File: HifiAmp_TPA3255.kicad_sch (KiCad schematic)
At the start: 111 parts, among them J1 PVDD 48V IN — NEEDS_DATA, J2 RCA L SE, J3 RCA R SE, J301 SPK_L, J302 SPK_R, Q301 NEEDS_DATA, U1 LM5010ASD, U2 LM2940IMP-12/NOPB, U3 TLV1117-33IDCY, U4 OPA1612AIDR, U5 OPA1612AIDR, U6 TPA3255B, U7 TPS3802K33DCKR

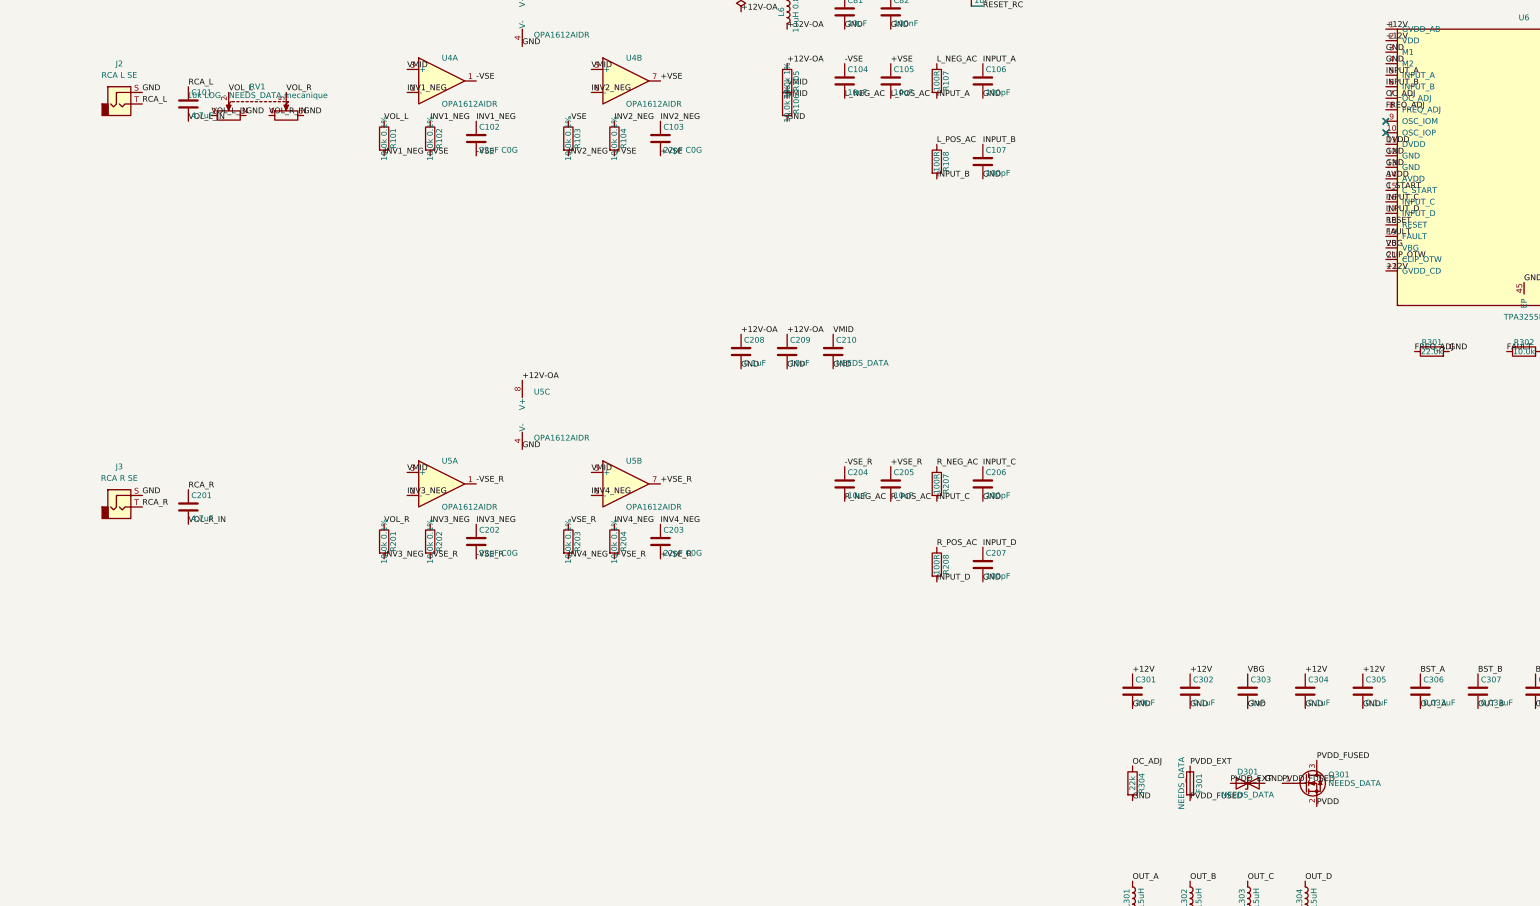
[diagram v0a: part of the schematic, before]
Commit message: feat(schematic): remote RV1/J2/J3, fix Q301 into a correct P-MOS (B2.1-B2.4)
J2/J3 become Conn_01x02 for chassis-mounted RCA, J4 (Conn_01x06) carries
the six volume nets for the remote pot, and Q301 is requalified from
N-MOS to P-MOS with a proper gate network (R305 100k to GND, D302 15 V
zener).

The first correction wired the P-MOS source upstream. A P-MOS body diode
has its anode on the drain, which must therefore sit upstream to conduct
in the normal direction; wired the other way the diode goes forward
during a polarity reversal and the protection does nothing. Verified
after fix by reading the symbol geometry: S carries PVDD, D carries
PVDD_FUSED, D302 cathode on PVDD. ERC cannot see this class of defect.

ERC re-gate: 0 errors / 14 warnings, 4 library mismatches + 10 off-grid,
same split as the C1 reference.

B2.1 stays open: no MCP tool exposes the on_board attribute, so RV1 is
still on the board (tracked as B2.8).

Co-Authored-By: Claude Opus 5 <noreply@anthropic.com>
Claude-Session: https://claude.ai/code/session_01NbP75MQx5stMnq6BjDMVex
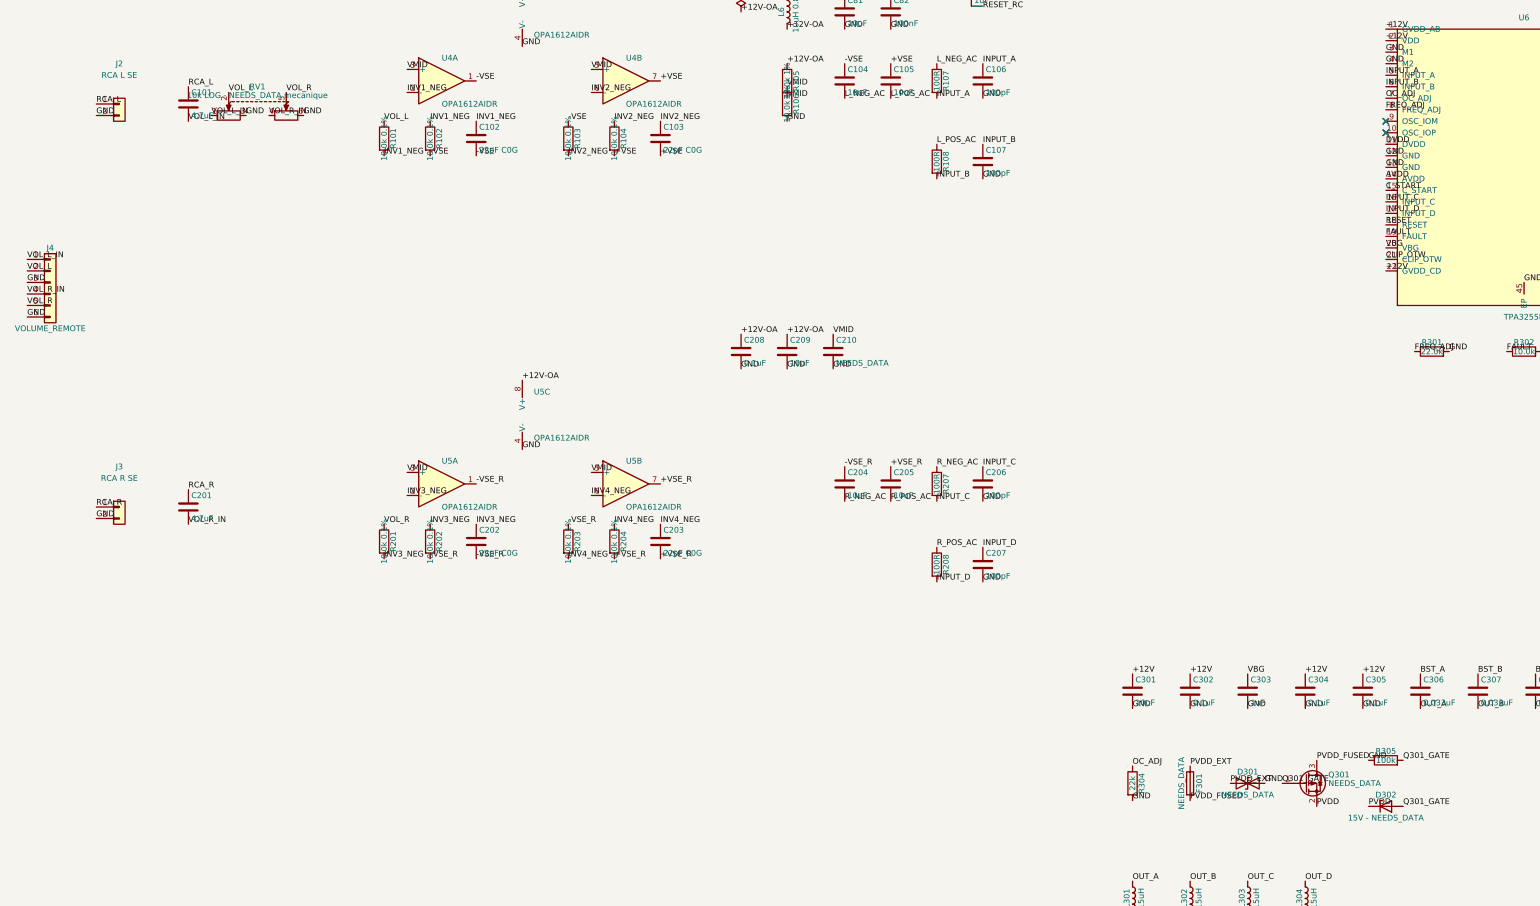
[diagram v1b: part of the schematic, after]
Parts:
- added D302: 15V - NEEDS_DATA, symbol Device:D_Zener
- added J4: VOLUME_REMOTE, symbol Connector_Generic:Conn_01x06
- added R305: 100k, symbol Device:R
- J2, J3: symbol Connector_Audio:AudioJack2 -> Connector_Generic:Conn_01x02
- Q301: symbol Transistor_FET:Q_NMOS_GSD -> Transistor_FET:Q_PMOS_GSD
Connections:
- net GND: now also J2.2 (Pin_2), J3.2 (Pin_2), J4.3 (Pin_3), J4.6 (Pin_6), R305.1; no longer J2.S, J3.S
- net PVDD: now also D302.1 (K)
- net PVDD_FUSED: no longer Q301.1 (G)
- net RCA_L: now also J2.1 (Pin_1); no longer J2.T
- net RCA_R: now also J3.1 (Pin_1); no longer J3.T
- net VOL_L: now also J4.2 (Pin_2)
- net VOL_L_IN: now also J4.1 (Pin_1)
- net VOL_R: now also J4.5 (Pin_5)
- net VOL_R_IN: now also J4.4 (Pin_4)
- new net Q301_GATE: D302.2 (A), Q301.1 (G), R305.2

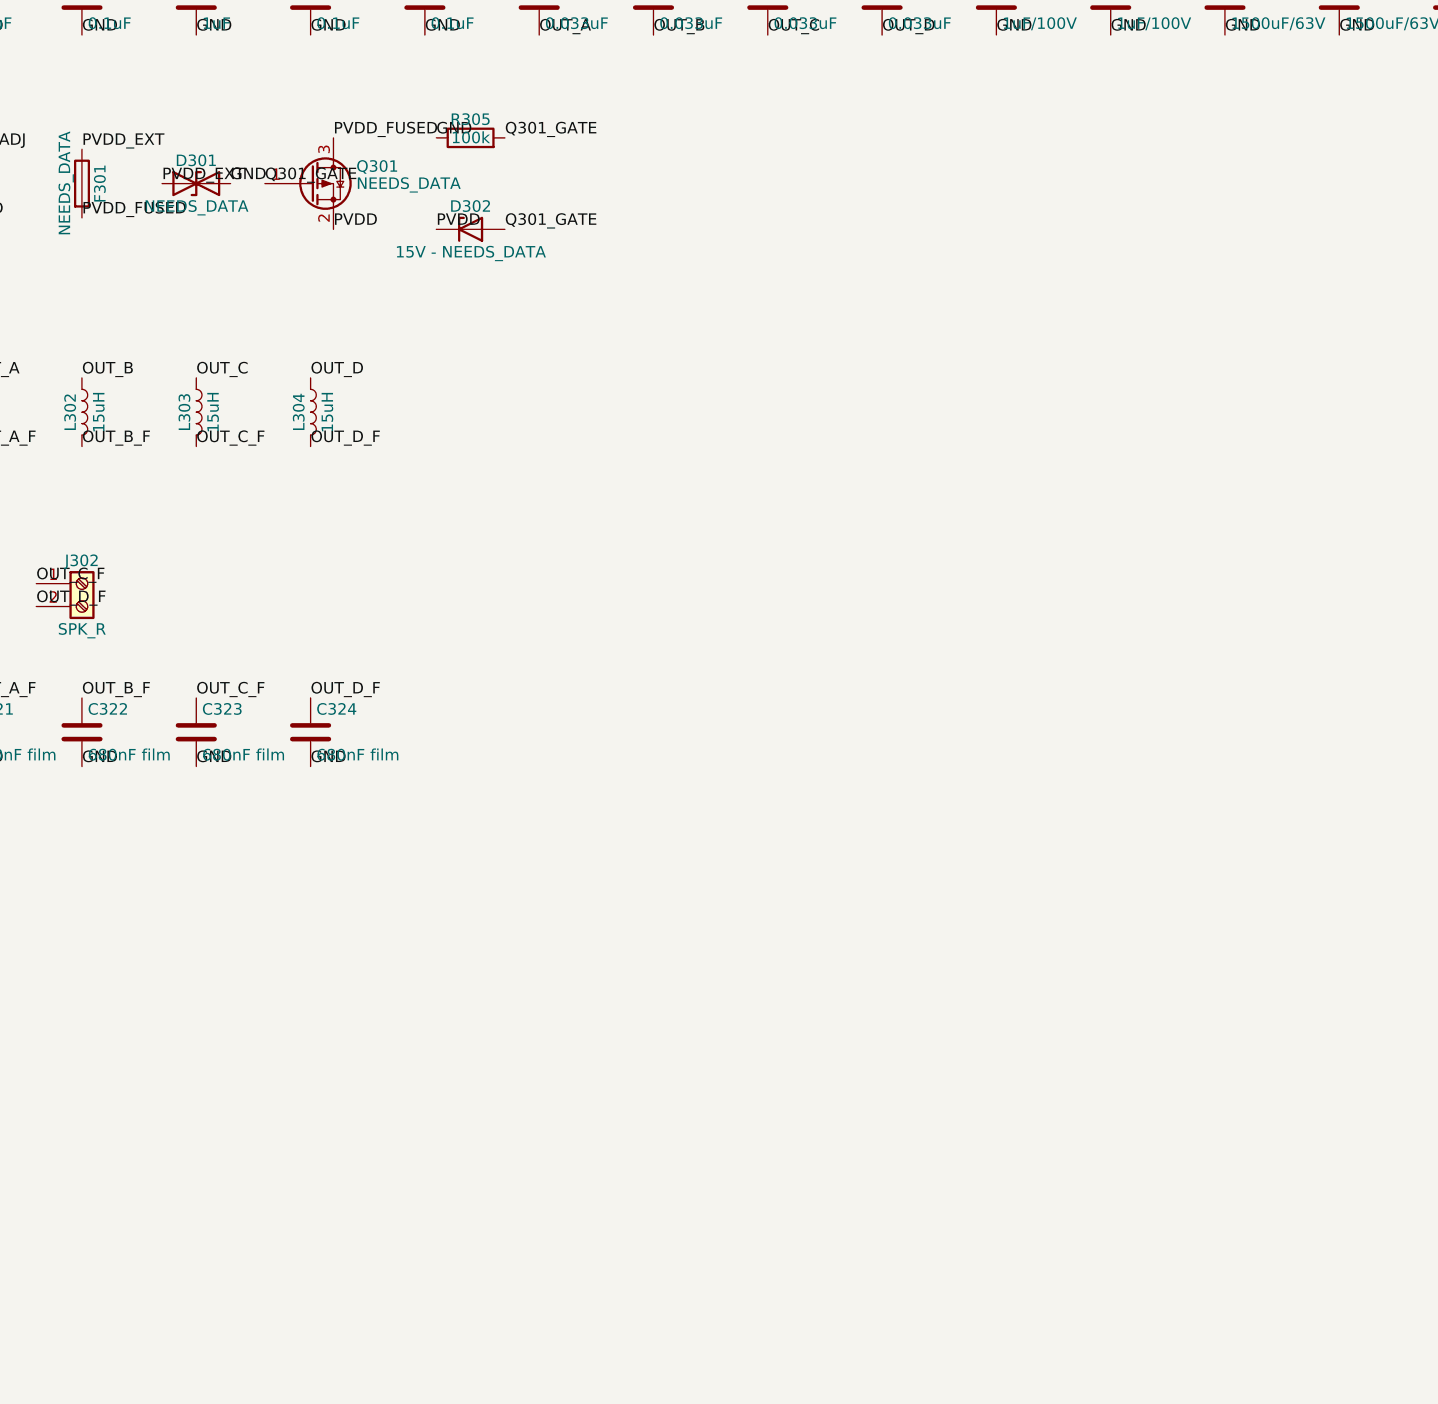
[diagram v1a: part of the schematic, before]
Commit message: feat(schematic): capture the LM5069 hot-swap block, C2 gate PASS (B2.6)
Inserts the active protection between Q301 and the bulk:
PVDD_FUSED -> Q301 -> PVDD_PROT -> R306 4m -> PVDD_SENSE -> Q302 -> PVDD.
U8 is an LM5069-2 with the Option A threshold divider (191k/5.11k/9.09k),
Rpwr 147k, Ctimer 3.9uF and a VIN bypass. The LM5069 symbol had to be
created locally: the stock library variants type TIMER as a plain input,
which is wrong for a pin that charges and discharges a capacitor.

Two ERC-invisible defects fixed:
- D301 sat upstream of F301. A TVS fails short, so upstream of the fuse
  it can short the source with no fuse able to clear it. Now on
  PVDD_FUSED, downstream of F301.
- PWR_FLAG added on PVDD_PROT, clearing the "Input Power pin not driven"
  error on U8 pin 2.

ERC: 0 errors / 15 warnings (5 library mismatches incl. the new U8,
10 off-grid). GATE C2 = PASS.

B2.5 stays blocked: the SOA requirement follows the bulk charge energy
(datasheet 9.2.1.1), so Q302 cannot be chosen until the bulk is settled.

Co-Authored-By: Claude Opus 5 <noreply@anthropic.com>
Claude-Session: https://claude.ai/code/session_01NbP75MQx5stMnq6BjDMVex
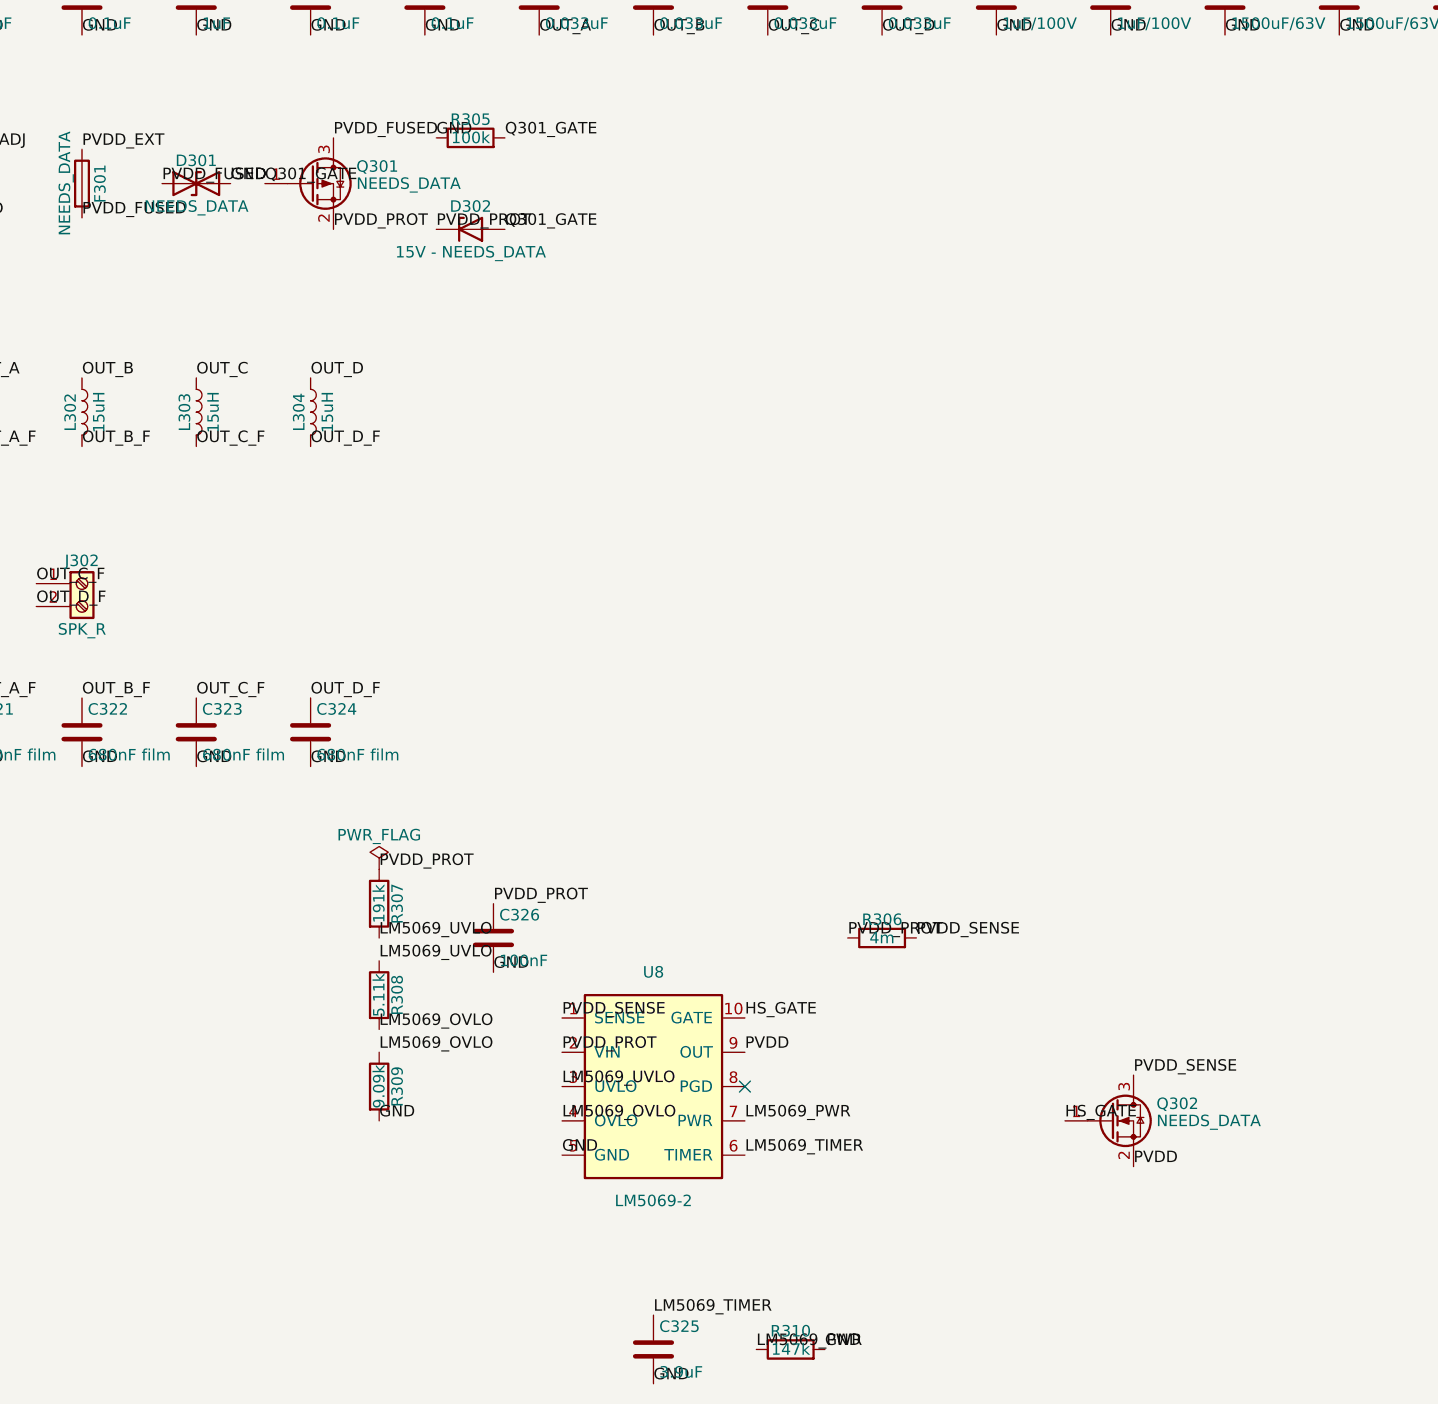
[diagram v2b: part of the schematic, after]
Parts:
- added C325: 3.9uF, symbol Device:C
- added C326: 100nF, symbol Device:C
- added Q302: NEEDS_DATA, symbol Transistor_FET:Q_NMOS_GSD
- added R306: 4m, symbol Device:R
- added R307: 191k, symbol Device:R
- added R308: 5.11k, symbol Device:R
- added R309: 9.09k, symbol Device:R
- added R310: 147k, symbol Device:R
- added U8: LM5069-2, Package_SO:MSOP-10_3x3mm_P0.5mm, symbol HifiAmp_TPA3255_Local:LM5069
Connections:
- net GND: now also C325.2, C326.2, R309.2, R310.2, U8.5 (GND)
- net PVDD: now also Q302.2 (S), U8.9 (OUT); no longer D302.1 (K), Q301.2 (S)
- net PVDD_EXT: no longer D301.1 (A1)
- net PVDD_FUSED: now also D301.1 (A1)
- new net HS_GATE: Q302.1 (G), U8.10 (GATE)
- new net LM5069_OVLO: R308.2, R309.1, U8.4 (OVLO)
- new net LM5069_PWR: R310.1, U8.7 (PWR)
- new net LM5069_TIMER: C325.1, U8.6 (TIMER)
- new net LM5069_UVLO: R307.2, R308.1, U8.3 (UVLO)
- new net PVDD_PROT: C326.1, D302.1 (K), Q301.2 (S), R306.1, R307.1, U8.2 (VIN)
- new net PVDD_SENSE: Q302.3 (D), R306.2, U8.1 (SENSE)
- no-connect marks 4 -> 5

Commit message: feat(protection): freeze Q302, F301 and D301 on read SOA curves (B2.5, B2.7)
Q302 = IXTK200N10L2, the only candidate whose guaranteed SOA covers the
389 W / 318 ms the 15400 uF bulk imposes. The obvious IXTH64N10L2 misses
by 1.8x: this bulk needs a die three times larger than 4.6 A suggests.

SOA curves are images, so both web searches came back empty on the one
number that mattered. Read them instead by extracting the PDF vector
paths and calibrating on the axis labels. Validated three ways: IDM
recovers as 140.2 A against 140 A in the table, and on all four
datasheets the derived value lands within 1% of the tested "Safe
Operating Area Specification" line.

IXYS publishes the curve at TC = 75 C directly, so the equation 19
derating is not needed at all.

F301 = Schurter UMT-H 12.5 A, 125 VDC with a stated DC breaking capacity.
A lower rating would break coordination: a legitimate LM5069 current
limit event is 1.23x In, for which the datasheet mandates >= 60 min
before arcing. The fuse is a last resort against a shorted Q302, never
overload protection.

D301 = SMDJ58A rather than SMCJ58A. LM5069 absolute maximum note (3) puts
GATE 12 V above VIN, so the service ceiling is 88 V, not 100 V. Both
clamp at 93.6 V but the 3000 W part does so at 32.1 A instead of 16.1 A.

New hard constraint recorded: Q301 must be rated VDS >= 100 V, since the
P-MOS carries the D301 clamp. Opened as B2.9.

Co-Authored-By: Claude Opus 5 <noreply@anthropic.com>
Claude-Session: https://claude.ai/code/session_01NUH7zQZvRu9pq1jvTrNHEG
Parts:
- D301: value NEEDS_DATA -> SMDJ58A; MPN (none) -> SMDJ58A
- F301: value NEEDS_DATA -> 12.5A T 125VDC; MPN (none) -> 3403.0285.11; Manufacturer (none) -> Schurter
- Q301: value NEEDS_DATA -> NEEDS_DATA - P-MOS VDS>=100V
- Q302: value NEEDS_DATA -> IXTK200N10L2; MPN (none) -> IXTK200N10L2; Manufacturer (none) -> Littelfuse/IXYS
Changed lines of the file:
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@@
 			)
 		)
-		(property "Value" "NEEDS_DATA"
+		(property "Value" "12.5A T 125VDC"
 			(at 264.795 320.04 90)
 			(effects
@@
 			)
 		)
+				(property "MPN" "3403.0285.11"
+			(at 266.7 320.04 0)
+			(effects (font (size 1.27 1.27)) (hide yes))
+		)
+				(property "Manufacturer" "Schurter"
+			(at 266.7 320.04 0)
+			(effects (font (size 1.27 1.27)) (hide yes))
+		)
 		(instances
 			(project "HifiAmp_TPA3255"
@@
 			)
 		)
-		(property "Value" "NEEDS_DATA"
+		(property "Value" "SMDJ58A"
 			(at 279.4 322.58 0)
 			(effects
@@
 			)
 		)
+				(property "MPN" "SMDJ58A"
+			(at 279.4 320.04 0)
+			(effects (font (size 1.27 1.27)) (hide yes))
+		)
 		(instances
 			(project "HifiAmp_TPA3255"
@@
 			)
 		)
-		(property "Value" "NEEDS_DATA"
+		(property "Value" "NEEDS_DATA - P-MOS VDS>=100V"
 			(at 297.18 320.04 0)
 			(effects
@@
 			)
 		)
-		(property "Value" "NEEDS_DATA"
+		(property "Value" "IXTK200N10L2"
 			(at 386.08 424.18 0)
 			(effects
@@
 			)
 		)
-		(instances
+				(property "MPN" "IXTK200N10L2"
+			(at 381 424.18 0)
+			(effects (font (size 1.27 1.27)) (hide yes))
+		)
+				(property "Manufacturer" "Littelfuse/IXYS"
+			(at 381 424.18 0)
+			(effects (font (size 1.27 1.27)) (hide yes))
+		)
+		(instances
